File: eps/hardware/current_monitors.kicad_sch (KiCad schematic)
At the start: 16 parts

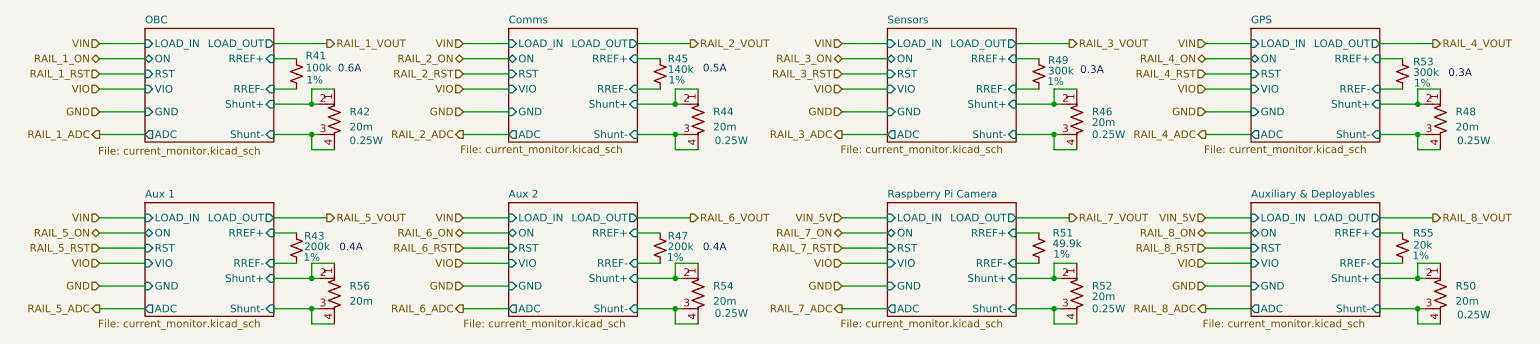
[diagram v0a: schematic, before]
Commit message: fix all ERC errors
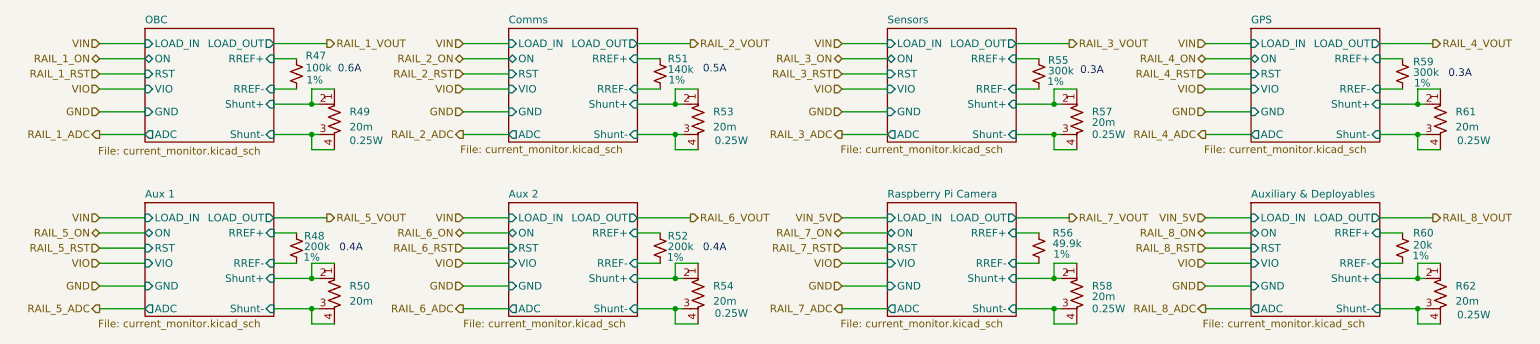
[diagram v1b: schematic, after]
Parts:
- renumbered R41 to R47, R43 to R48, R42 to R49, R56 to R50, R45 to R51, R47 to R52, R44 to R53, R49 to R55, R51 to R56, R46 to R57, R52 to R58, R53 to R59, R55 to R60, R48 to R61, R50 to R62
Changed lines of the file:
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@@
 		(on_board yes)
 		(dnp no)
-		(property "Reference" "R53"
+		(property "Reference" "R59"
 			(at 255.778 23.368 0)
 			(effects
@@
 			(project "eps"
 				(path "/9e0ae2e7-d4be-41b4-8312-0d2aceea2180/373e68a1-9d85-40af-a211-fd16b724d579"
-					(reference "R53")
+					(reference "R59")
 					(unit 1)
 				)
@@
 		(on_board yes)
 		(dnp no)
-		(property "Reference" "R41"
+		(property "Reference" "R47"
 			(at 70.104 22.352 0)
 			(effects
@@
 			(project "eps"
 				(path "/9e0ae2e7-d4be-41b4-8312-0d2aceea2180/373e68a1-9d85-40af-a211-fd16b724d579"
-					(reference "R41")
+					(reference "R47")
 					(unit 1)
 				)
@@
 		(on_board yes)
 		(dnp no)
-		(property "Reference" "R43"
+		(property "Reference" "R48"
 			(at 69.85 52.578 0)
 			(effects
@@
 			(project "eps"
 				(path "/9e0ae2e7-d4be-41b4-8312-0d2aceea2180/373e68a1-9d85-40af-a211-fd16b724d579"
-					(reference "R43")
+					(reference "R48")
 					(unit 1)
 				)
@@
 		(on_board yes)
 		(dnp no)
-		(property "Reference" "R48"
+		(property "Reference" "R61"
 			(at 262.89 31.7499 0)
 			(effects
@@
 			(project "eps"
 				(path "/9e0ae2e7-d4be-41b4-8312-0d2aceea2180/373e68a1-9d85-40af-a211-fd16b724d579"
-					(reference "R48")
+					(reference "R61")
 					(unit 1)
 				)
@@
 		(on_board yes)
 		(dnp no)
-		(property "Reference" "R52"
+		(property "Reference" "R58"
 			(at 201.93 60.9599 0)
 			(effects
@@
 			(project "eps"
 				(path "/9e0ae2e7-d4be-41b4-8312-0d2aceea2180/373e68a1-9d85-40af-a211-fd16b724d579"
-					(reference "R52")
+					(reference "R58")
 					(unit 1)
 				)
@@
 		(on_board yes)
 		(dnp no)
-		(property "Reference" "R44"
+		(property "Reference" "R53"
 			(at 138.43 31.7499 0)
 			(effects
@@
 			(project "eps"
 				(path "/9e0ae2e7-d4be-41b4-8312-0d2aceea2180/373e68a1-9d85-40af-a211-fd16b724d579"
-					(reference "R44")
+					(reference "R53")
 					(unit 1)
 				)
@@
 		(on_board yes)
 		(dnp no)
-		(property "Reference" "R46"
+		(property "Reference" "R57"
 			(at 201.93 31.7499 0)
 			(effects
@@
 			(project "eps"
 				(path "/9e0ae2e7-d4be-41b4-8312-0d2aceea2180/373e68a1-9d85-40af-a211-fd16b724d579"
-					(reference "R46")
+					(reference "R57")
 					(unit 1)
 				)
@@
 		(dnp no)
 		(fields_autoplaced yes)
-		(property "Reference" "R56"
+		(property "Reference" "R50"
 			(at 77.47 60.9599 0)
 			(effects
@@
 			(project "eps"
 				(path "/9e0ae2e7-d4be-41b4-8312-0d2aceea2180/373e68a1-9d85-40af-a211-fd16b724d579"
-					(reference "R56")
+					(reference "R50")
 					(unit 1)
 				)
@@
 		(on_board yes)
 		(dnp no)
-		(property "Reference" "R55"
+		(property "Reference" "R60"
 			(at 255.778 52.07 0)
 			(effects
@@
 			(project "eps"
 				(path "/9e0ae2e7-d4be-41b4-8312-0d2aceea2180/373e68a1-9d85-40af-a211-fd16b724d579"
-					(reference "R55")
+					(reference "R60")
 					(unit 1)
 				)
@@
 		(on_board yes)
 		(dnp no)
-		(property "Reference" "R42"
+		(property "Reference" "R49"
 			(at 77.47 31.7499 0)
 			(effects
@@
 			(project ""
 				(path "/9e0ae2e7-d4be-41b4-8312-0d2aceea2180/373e68a1-9d85-40af-a211-fd16b724d579"
-					(reference "R42")
+					(reference "R49")
 					(unit 1)
 				)
@@
 		(on_board yes)
 		(dnp no)
-		(property "Reference" "R49"
+		(property "Reference" "R55"
 			(at 194.564 23.114 0)
 			(effects
@@
 			(project "eps"
 				(path "/9e0ae2e7-d4be-41b4-8312-0d2aceea2180/373e68a1-9d85-40af-a211-fd16b724d579"
-					(reference "R49")
+					(reference "R55")
 					(unit 1)
 				)
@@
 		(on_board yes)
 		(dnp no)
-		(property "Reference" "R47"
+		(property "Reference" "R52"
 			(at 130.81 52.578 0)
 			(effects
@@
 			(project "eps"
 				(path "/9e0ae2e7-d4be-41b4-8312-0d2aceea2180/373e68a1-9d85-40af-a211-fd16b724d579"
-					(reference "R47")
+					(reference "R52")
 					(unit 1)
 				)
@@
 		(on_board yes)
 		(dnp no)
-		(property "Reference" "R51"
+		(property "Reference" "R56"
 			(at 195.326 52.07 0)
 			(effects
@@
 			(project "eps"
 				(path "/9e0ae2e7-d4be-41b4-8312-0d2aceea2180/373e68a1-9d85-40af-a211-fd16b724d579"
-					(reference "R51")
+					(reference "R56")
 					(unit 1)
 				)
@@
 		(on_board yes)
 		(dnp no)
-		(property "Reference" "R45"
+		(property "Reference" "R51"
 			(at 130.81 22.86 0)
 			(effects
@@
 			(project "eps"
 				(path "/9e0ae2e7-d4be-41b4-8312-0d2aceea2180/373e68a1-9d85-40af-a211-fd16b724d579"
-					(reference "R45")
+					(reference "R51")
 					(unit 1)
 				)
@@
 		(on_board yes)
 		(dnp no)
-		(property "Reference" "R50"
+		(property "Reference" "R62"
 			(at 262.89 60.9599 0)
 			(effects
@@
 			(project "eps"
 				(path "/9e0ae2e7-d4be-41b4-8312-0d2aceea2180/373e68a1-9d85-40af-a211-fd16b724d579"
-					(reference "R50")
-					(unit 1)
-				)
+					(reference "R62")
+					(unit 1)
+				)

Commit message: netlist fixes
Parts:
- renumbered R47 to R35, R48 to R36, R49 to R37, R50 to R38, R51 to R39, R52 to R40, R53 to R41, R54 to R42, R55 to R43, R56 to R44, R57 to R45, R58 to R46, R59 to R47, R60 to R48, R61 to R49, R62 to R50
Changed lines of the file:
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@@
 		(on_board yes)
 		(dnp no)
-		(property "Reference" "R59"
+		(property "Reference" "R47"
 			(at 255.778 23.368 0)
 			(effects
@@
 			(project "eps"
 				(path "/9e0ae2e7-d4be-41b4-8312-0d2aceea2180/373e68a1-9d85-40af-a211-fd16b724d579"
-					(reference "R59")
+					(reference "R47")
 					(unit 1)
 				)
@@
 		(on_board yes)
 		(dnp no)
-		(property "Reference" "R47"
+		(property "Reference" "R35"
 			(at 70.104 22.352 0)
 			(effects
@@
 			(project "eps"
 				(path "/9e0ae2e7-d4be-41b4-8312-0d2aceea2180/373e68a1-9d85-40af-a211-fd16b724d579"
-					(reference "R47")
+					(reference "R35")
 					(unit 1)
 				)
@@
 		(on_board yes)
 		(dnp no)
-		(property "Reference" "R48"
+		(property "Reference" "R36"
 			(at 69.85 52.578 0)
 			(effects
@@
 			(project "eps"
 				(path "/9e0ae2e7-d4be-41b4-8312-0d2aceea2180/373e68a1-9d85-40af-a211-fd16b724d579"
-					(reference "R48")
+					(reference "R36")
 					(unit 1)
 				)
@@
 		(on_board yes)
 		(dnp no)
-		(property "Reference" "R61"
+		(property "Reference" "R49"
 			(at 262.89 31.7499 0)
 			(effects
@@
 			(project "eps"
 				(path "/9e0ae2e7-d4be-41b4-8312-0d2aceea2180/373e68a1-9d85-40af-a211-fd16b724d579"
-					(reference "R61")
+					(reference "R49")
 					(unit 1)
 				)
@@
 		(on_board yes)
 		(dnp no)
-		(property "Reference" "R58"
+		(property "Reference" "R46"
 			(at 201.93 60.9599 0)
 			(effects
@@
 			(project "eps"
 				(path "/9e0ae2e7-d4be-41b4-8312-0d2aceea2180/373e68a1-9d85-40af-a211-fd16b724d579"
-					(reference "R58")
+					(reference "R46")
 					(unit 1)
 				)
@@
 		(on_board yes)
 		(dnp no)
-		(property "Reference" "R53"
+		(property "Reference" "R41"
 			(at 138.43 31.7499 0)
 			(effects
@@
 			(project "eps"
 				(path "/9e0ae2e7-d4be-41b4-8312-0d2aceea2180/373e68a1-9d85-40af-a211-fd16b724d579"
-					(reference "R53")
+					(reference "R41")
 					(unit 1)
 				)
@@
 		(on_board yes)
 		(dnp no)
-		(property "Reference" "R57"
+		(property "Reference" "R45"
 			(at 201.93 31.7499 0)
 			(effects
@@
 			(project "eps"
 				(path "/9e0ae2e7-d4be-41b4-8312-0d2aceea2180/373e68a1-9d85-40af-a211-fd16b724d579"
-					(reference "R57")
+					(reference "R45")
 					(unit 1)
 				)
@@
 		(dnp no)
 		(fields_autoplaced yes)
-		(property "Reference" "R50"
+		(property "Reference" "R38"
 			(at 77.47 60.9599 0)
 			(effects
@@
 			(project "eps"
 				(path "/9e0ae2e7-d4be-41b4-8312-0d2aceea2180/373e68a1-9d85-40af-a211-fd16b724d579"
-					(reference "R50")
+					(reference "R38")
 					(unit 1)
 				)
@@
 		(on_board yes)
 		(dnp no)
-		(property "Reference" "R60"
+		(property "Reference" "R48"
 			(at 255.778 52.07 0)
 			(effects
@@
 			(project "eps"
 				(path "/9e0ae2e7-d4be-41b4-8312-0d2aceea2180/373e68a1-9d85-40af-a211-fd16b724d579"
-					(reference "R60")
+					(reference "R48")
 					(unit 1)
 				)
@@
 		(on_board yes)
 		(dnp no)
-		(property "Reference" "R49"
+		(property "Reference" "R37"
 			(at 77.47 31.7499 0)
 			(effects
@@
 			(project ""
 				(path "/9e0ae2e7-d4be-41b4-8312-0d2aceea2180/373e68a1-9d85-40af-a211-fd16b724d579"
-					(reference "R49")
+					(reference "R37")
 					(unit 1)
 				)
@@
 		(on_board yes)
 		(dnp no)
-		(property "Reference" "R55"
+		(property "Reference" "R43"
 			(at 194.564 23.114 0)
 			(effects
@@
 			(project "eps"
 				(path "/9e0ae2e7-d4be-41b4-8312-0d2aceea2180/373e68a1-9d85-40af-a211-fd16b724d579"
-					(reference "R55")
+					(reference "R43")
 					(unit 1)
 				)
@@
 		(on_board yes)
 		(dnp no)
-		(property "Reference" "R52"
+		(property "Reference" "R40"
 			(at 130.81 52.578 0)
 			(effects
@@
 			(project "eps"
 				(path "/9e0ae2e7-d4be-41b4-8312-0d2aceea2180/373e68a1-9d85-40af-a211-fd16b724d579"
-					(reference "R52")
+					(reference "R40")
 					(unit 1)
 				)
@@
 		(on_board yes)
 		(dnp no)
-		(property "Reference" "R56"
+		(property "Reference" "R44"
 			(at 195.326 52.07 0)
 			(effects
@@
 			(project "eps"
 				(path "/9e0ae2e7-d4be-41b4-8312-0d2aceea2180/373e68a1-9d85-40af-a211-fd16b724d579"
-					(reference "R56")
+					(reference "R44")
 					(unit 1)
 				)
@@
 		(on_board yes)
 		(dnp no)
-		(property "Reference" "R54"
+		(property "Reference" "R42"
 			(at 138.43 60.9599 0)
 			(effects
@@
 			(project "eps"
 				(path "/9e0ae2e7-d4be-41b4-8312-0d2aceea2180/373e68a1-9d85-40af-a211-fd16b724d579"
-					(reference "R54")
+					(reference "R42")
 					(unit 1)
 				)
@@
 		(on_board yes)
 		(dnp no)
-		(property "Reference" "R51"
+		(property "Reference" "R39"
 			(at 130.81 22.86 0)
 			(effects
@@
 			(project "eps"
 				(path "/9e0ae2e7-d4be-41b4-8312-0d2aceea2180/373e68a1-9d85-40af-a211-fd16b724d579"
-					(reference "R51")
+					(reference "R39")
 					(unit 1)
 				)
@@
 		(on_board yes)
 		(dnp no)
-		(property "Reference" "R62"
+		(property "Reference" "R50"
 			(at 262.89 60.9599 0)
 			(effects
@@
 			(project "eps"
 				(path "/9e0ae2e7-d4be-41b4-8312-0d2aceea2180/373e68a1-9d85-40af-a211-fd16b724d579"
-					(reference "R62")
-					(unit 1)
-				)
+					(reference "R50")
+					(unit 1)
+				)

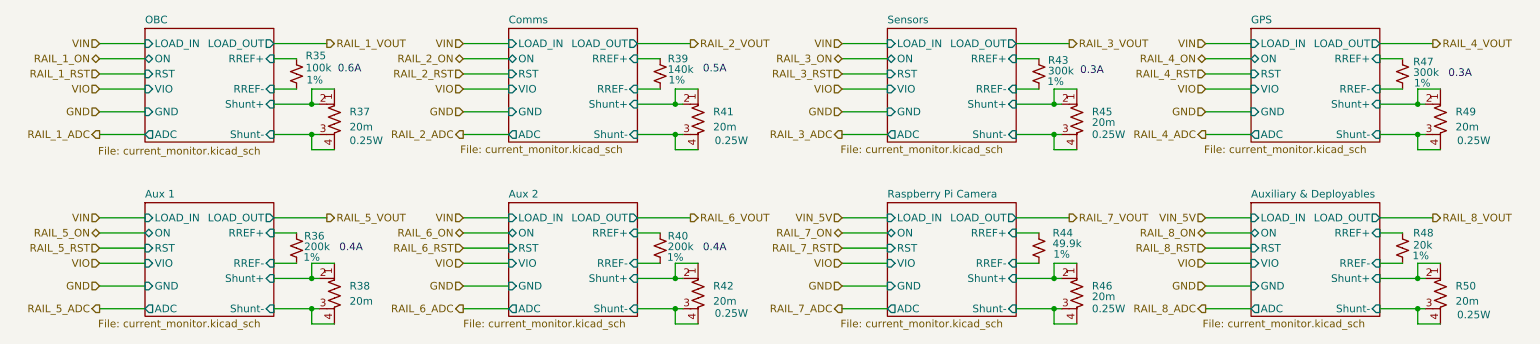
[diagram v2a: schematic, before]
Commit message: change battery cells to connector
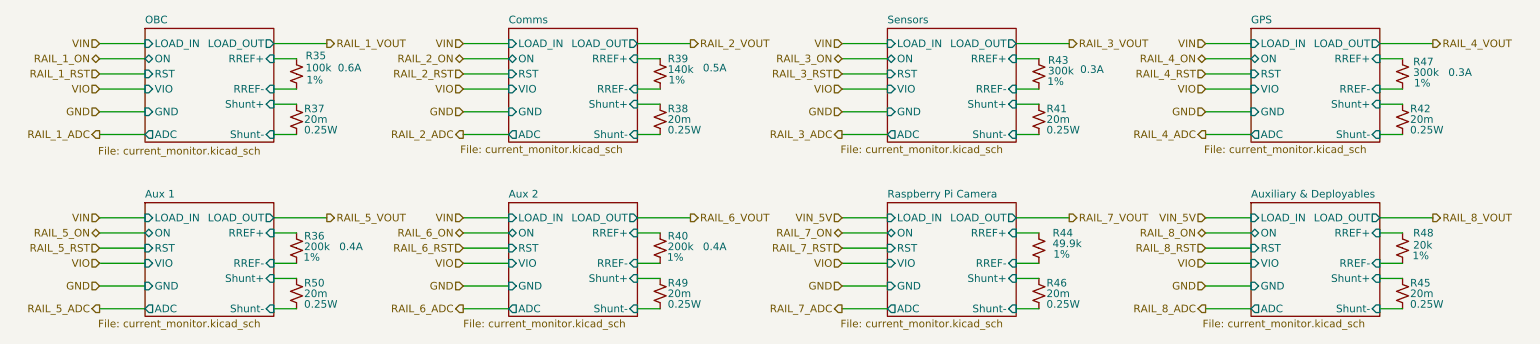
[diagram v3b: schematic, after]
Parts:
- removed R37, R38, R41, R42, R45, R46, R49, R50: 20m, symbol Device:R_Shunt_US
- added R37, R38, R41, R42, R45, R46, R49, R50: 20m, symbol Device:R_Small_US
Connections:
- net Aux 1/Shunt+: now also R50.1
- net Aux 1/Shunt-: now also R50.2
- net Aux 2/Shunt+: now also R49.1
- net Aux 2/Shunt-: now also R49.2
- net Auxiliary & Deployables/Shunt+: now also R45.1
- net Auxiliary & Deployables/Shunt-: now also R45.2
- net Comms/Shunt+: now also R38.1
- net Comms/Shunt-: now also R38.2
- net GPS/Shunt+: now also R42.1
- net GPS/Shunt-: now also R42.2
- net OBC/Shunt+: now also R37.1
- net OBC/Shunt-: now also R37.2
- net Raspberry Pi Camera/Shunt+: now also R46.1
- net Raspberry Pi Camera/Shunt-: now also R46.2
- net Sensors/Shunt+: now also R41.1
- net Sensors/Shunt-: now also R41.2

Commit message: finish footprint assignment and board setup
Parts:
- R35, R36, R37, R38, R39, R40, R41, R42, R43, R44, R45, R46, R47, R48, R49, R50: footprint (none) -> Resistor_SMD:R_0603_1608Metric
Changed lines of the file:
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@@
 			)
 		)
-		(property "Footprint" ""
+		(property "Footprint" "Resistor_SMD:R_0603_1608Metric"
 			(at 129.54 62.23 0)
 			(effects
@@
 			)
 		)
-		(property "Footprint" ""
+		(property "Footprint" "Resistor_SMD:R_0603_1608Metric"
 			(at 254 25.4 0)
 			(effects
@@
 			)
 		)
-		(property "Footprint" ""
+		(property "Footprint" "Resistor_SMD:R_0603_1608Metric"
 			(at 68.58 25.4 0)
 			(effects
@@
 			)
 		)
-		(property "Footprint" ""
+		(property "Footprint" "Resistor_SMD:R_0603_1608Metric"
 			(at 68.58 54.61 0)
 			(effects
@@
 			)
 		)
-		(property "Footprint" ""
+		(property "Footprint" "Resistor_SMD:R_0603_1608Metric"
 			(at 129.54 33.02 0)
 			(effects
@@
 			)
 		)
-		(property "Footprint" ""
+		(property "Footprint" "Resistor_SMD:R_0603_1608Metric"
 			(at 68.58 33.02 0)
 			(effects
@@
 			)
 		)
-		(property "Footprint" ""
+		(property "Footprint" "Resistor_SMD:R_0603_1608Metric"
 			(at 254 33.02 0)
 			(effects
@@
 			)
 		)
-		(property "Footprint" ""
+		(property "Footprint" "Resistor_SMD:R_0603_1608Metric"
 			(at 254 54.61 0)
 			(effects
@@
 			)
 		)
-		(property "Footprint" ""
+		(property "Footprint" "Resistor_SMD:R_0603_1608Metric"
 			(at 193.04 62.23 0)
 			(effects
@@
 			)
 		)
-		(property "Footprint" ""
+		(property "Footprint" "Resistor_SMD:R_0603_1608Metric"
 			(at 254 62.23 0)
 			(effects
@@
 			)
 		)
-		(property "Footprint" ""
+		(property "Footprint" "Resistor_SMD:R_0603_1608Metric"
 			(at 193.04 25.4 0)
 			(effects
@@
 			)
 		)
-		(property "Footprint" ""
+		(property "Footprint" "Resistor_SMD:R_0603_1608Metric"
 			(at 129.54 54.61 0)
 			(effects
@@
 			)
 		)
-		(property "Footprint" ""
+		(property "Footprint" "Resistor_SMD:R_0603_1608Metric"
 			(at 68.58 62.23 0)
 			(effects
@@
 			)
 		)
-		(property "Footprint" ""
+		(property "Footprint" "Resistor_SMD:R_0603_1608Metric"
 			(at 193.04 54.61 0)
 			(effects
@@
 			)
 		)
-		(property "Footprint" ""
+		(property "Footprint" "Resistor_SMD:R_0603_1608Metric"
 			(at 129.54 25.4 0)
 			(effects
@@
 			)
 		)
-		(property "Footprint" ""
+		(property "Footprint" "Resistor_SMD:R_0603_1608Metric"
 			(at 193.04 33.02 0)
 			(effects

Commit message: schematic fixes
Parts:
- R35, R36, R37, R38, R39, R40, R41, R42, R43, R44, R45, R46, R47, R48, R49, R50: footprint Resistor_SMD:R_0603_1608Metric -> Resistor_SMD:R_0402_1005Metric
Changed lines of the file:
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@@
 			)
 		)
-		(property "Footprint" "Resistor_SMD:R_0603_1608Metric"
+		(property "Footprint" "Resistor_SMD:R_0402_1005Metric"
 			(at 129.54 62.23 0)
 			(effects
@@
 			)
 		)
-		(property "Footprint" "Resistor_SMD:R_0603_1608Metric"
+		(property "Footprint" "Resistor_SMD:R_0402_1005Metric"
 			(at 254 25.4 0)
 			(effects
@@
 			)
 		)
-		(property "Footprint" "Resistor_SMD:R_0603_1608Metric"
+		(property "Footprint" "Resistor_SMD:R_0402_1005Metric"
 			(at 68.58 25.4 0)
 			(effects
@@
 			)
 		)
-		(property "Footprint" "Resistor_SMD:R_0603_1608Metric"
+		(property "Footprint" "Resistor_SMD:R_0402_1005Metric"
 			(at 68.58 54.61 0)
 			(effects
@@
 			)
 		)
-		(property "Footprint" "Resistor_SMD:R_0603_1608Metric"
+		(property "Footprint" "Resistor_SMD:R_0402_1005Metric"
 			(at 129.54 33.02 0)
 			(effects
@@
 			)
 		)
-		(property "Footprint" "Resistor_SMD:R_0603_1608Metric"
+		(property "Footprint" "Resistor_SMD:R_0402_1005Metric"
 			(at 68.58 33.02 0)
 			(effects
@@
 			)
 		)
-		(property "Footprint" "Resistor_SMD:R_0603_1608Metric"
+		(property "Footprint" "Resistor_SMD:R_0402_1005Metric"
 			(at 254 33.02 0)
 			(effects
@@
 			)
 		)
-		(property "Footprint" "Resistor_SMD:R_0603_1608Metric"
+		(property "Footprint" "Resistor_SMD:R_0402_1005Metric"
 			(at 254 54.61 0)
 			(effects
@@
 			)
 		)
-		(property "Footprint" "Resistor_SMD:R_0603_1608Metric"
+		(property "Footprint" "Resistor_SMD:R_0402_1005Metric"
 			(at 193.04 62.23 0)
 			(effects
@@
 			)
 		)
-		(property "Footprint" "Resistor_SMD:R_0603_1608Metric"
+		(property "Footprint" "Resistor_SMD:R_0402_1005Metric"
 			(at 254 62.23 0)
 			(effects
@@
 			)
 		)
-		(property "Footprint" "Resistor_SMD:R_0603_1608Metric"
+		(property "Footprint" "Resistor_SMD:R_0402_1005Metric"
 			(at 193.04 25.4 0)
 			(effects
@@
 			)
 		)
-		(property "Footprint" "Resistor_SMD:R_0603_1608Metric"
+		(property "Footprint" "Resistor_SMD:R_0402_1005Metric"
 			(at 129.54 54.61 0)
 			(effects
@@
 			)
 		)
-		(property "Footprint" "Resistor_SMD:R_0603_1608Metric"
+		(property "Footprint" "Resistor_SMD:R_0402_1005Metric"
 			(at 68.58 62.23 0)
 			(effects
@@
 			)
 		)
-		(property "Footprint" "Resistor_SMD:R_0603_1608Metric"
+		(property "Footprint" "Resistor_SMD:R_0402_1005Metric"
 			(at 193.04 54.61 0)
 			(effects
@@
 			)
 		)
-		(property "Footprint" "Resistor_SMD:R_0603_1608Metric"
+		(property "Footprint" "Resistor_SMD:R_0402_1005Metric"
 			(at 129.54 25.4 0)
 			(effects
@@
 			)
 		)
-		(property "Footprint" "Resistor_SMD:R_0603_1608Metric"
+		(property "Footprint" "Resistor_SMD:R_0402_1005Metric"
 			(at 193.04 33.02 0)
 			(effects

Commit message: change footprint sizes for current monitoring
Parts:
- R37, R38, R41, R42, R45, R46, R49, R50: footprint Resistor_SMD:R_0402_1005Metric -> Resistor_SMD:R_1206_3216Metric
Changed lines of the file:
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@@
 			)
 		)
-		(property "Footprint" "Resistor_SMD:R_0402_1005Metric"
+		(property "Footprint" "Resistor_SMD:R_1206_3216Metric"
 			(at 129.54 62.23 0)
 			(effects
@@
 			)
 		)
-		(property "Footprint" "Resistor_SMD:R_0402_1005Metric"
+		(property "Footprint" "Resistor_SMD:R_1206_3216Metric"
 			(at 129.54 33.02 0)
 			(effects
@@
 			)
 		)
-		(property "Footprint" "Resistor_SMD:R_0402_1005Metric"
+		(property "Footprint" "Resistor_SMD:R_1206_3216Metric"
 			(at 68.58 33.02 0)
 			(effects
@@
 			)
 		)
-		(property "Footprint" "Resistor_SMD:R_0402_1005Metric"
+		(property "Footprint" "Resistor_SMD:R_1206_3216Metric"
 			(at 254 33.02 0)
 			(effects
@@
 			)
 		)
-		(property "Footprint" "Resistor_SMD:R_0402_1005Metric"
+		(property "Footprint" "Resistor_SMD:R_1206_3216Metric"
 			(at 193.04 62.23 0)
 			(effects
@@
 			)
 		)
-		(property "Footprint" "Resistor_SMD:R_0402_1005Metric"
+		(property "Footprint" "Resistor_SMD:R_1206_3216Metric"
 			(at 254 62.23 0)
 			(effects
@@
 			)
 		)
-		(property "Footprint" "Resistor_SMD:R_0402_1005Metric"
+		(property "Footprint" "Resistor_SMD:R_1206_3216Metric"
 			(at 68.58 62.23 0)
 			(effects
@@
 			)
 		)
-		(property "Footprint" "Resistor_SMD:R_0402_1005Metric"
+		(property "Footprint" "Resistor_SMD:R_1206_3216Metric"
 			(at 193.04 33.02 0)
 			(effects
